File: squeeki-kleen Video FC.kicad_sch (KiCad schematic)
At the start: 11 parts, among them J1 VCC, J2 VOUT, J3 GND, J4 Conn_Coaxial, Q1 MMBT3906

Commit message: Add version number to PCB
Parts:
- J4: now left out of the parts list
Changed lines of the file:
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@@
   )
   (symbol (lib_id "Connector:Conn_Coaxial") (at 105.41 31.75 0) (unit 1)
-    (in_bom yes) (on_board yes) (dnp no) (fields_autoplaced)
+    (in_bom no) (on_board yes) (dnp no) (fields_autoplaced)
     (property "Reference" "J4" (at 107.95 30.7731 0)
       (effects (font (size 1.27 1.27)) (justify left))

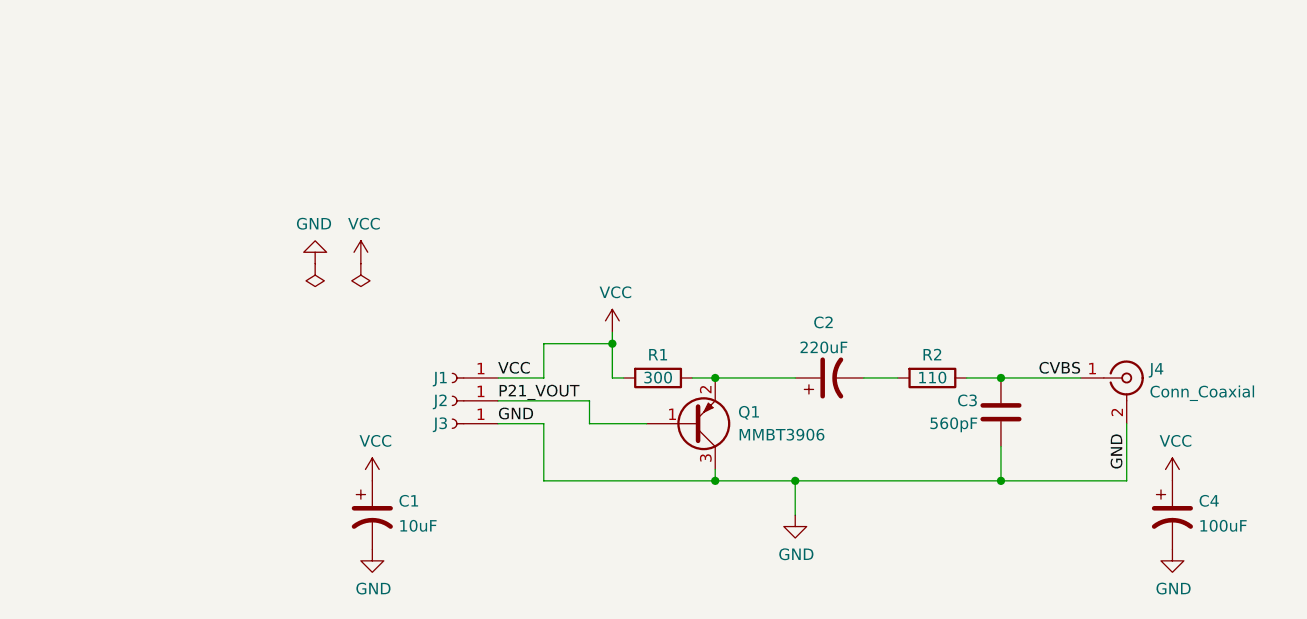
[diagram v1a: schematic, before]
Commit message: Compact component placement, add teardrops
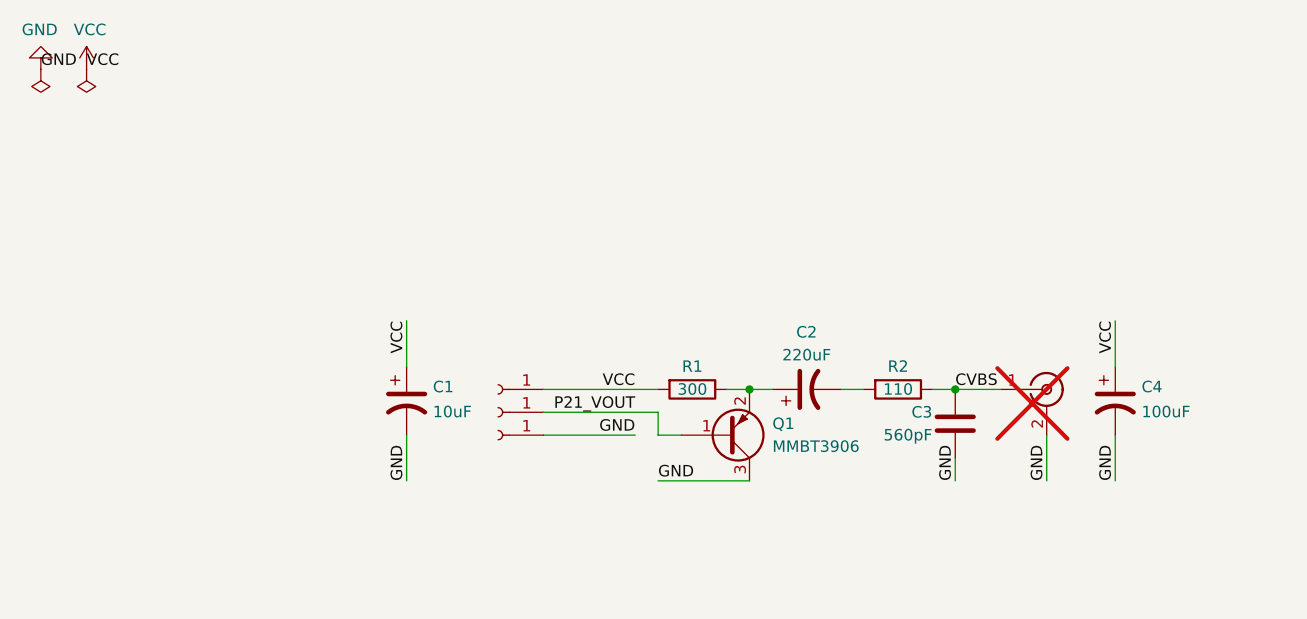
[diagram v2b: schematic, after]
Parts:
- C1: footprint Capacitor_Tantalum_SMD:CP_EIA-3216-18_Kemet-A_Pad1.58x1.35mm_HandSolder -> Capacitor_Tantalum_SMD:CP_EIA-3216-18_Kemet-A
- C3: footprint Capacitor_SMD:C_0805_2012Metric_Pad1.18x1.45mm_HandSolder -> Capacitor_SMD:C_0805_2012Metric
- C4: LCSC C1508940 -> C5374788
- J1, J2, J3: now left out of the parts list
- J4: now not fitted
- Q1: LCSC (none) -> C2891809
- R1, R2: footprint Resistor_SMD:R_0805_2012Metric_Pad1.20x1.40mm_HandSolder -> Resistor_SMD:R_0805_2012Metric
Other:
- moved on the sheet: C1, C2, C3, C4, Q1, R1, R2

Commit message: Widen holes, add extra empty capacitor footprints
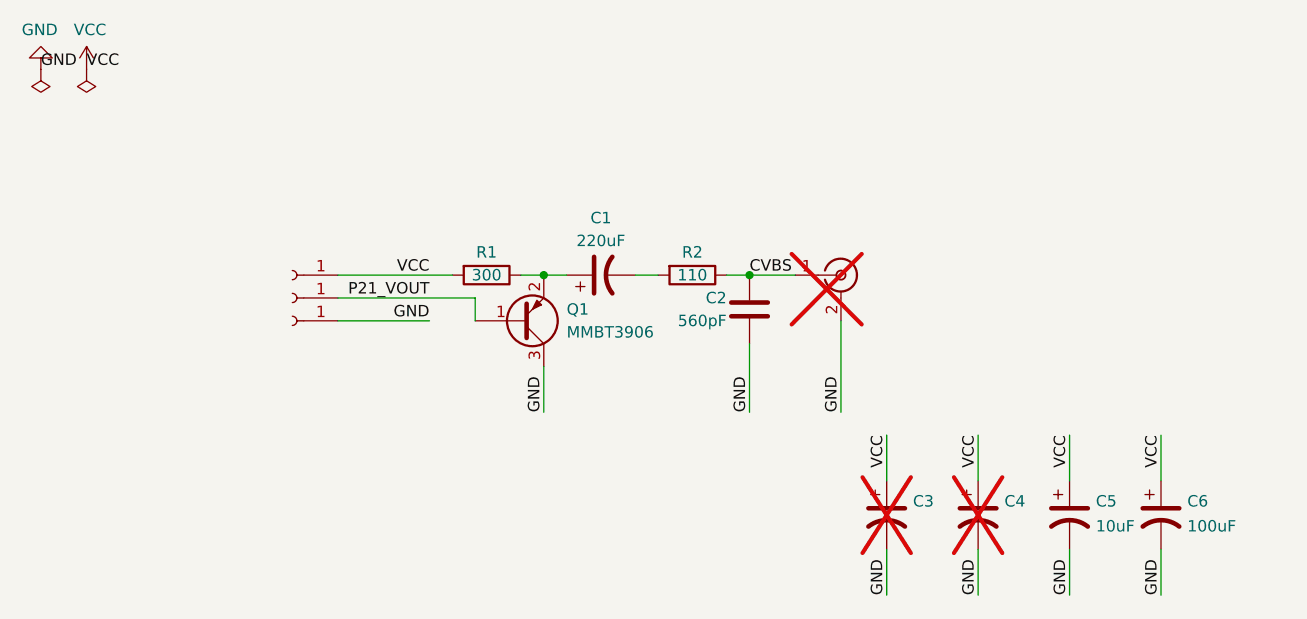
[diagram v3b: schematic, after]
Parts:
- added C3, C4: ~, Capacitor_Tantalum_SMD:CP_EIA-3216-18_Kemet-A, symbol Device:C_Polarized_US
- renumbered C2 to C1, C3 to C2, C1 to C5, C4 to C6
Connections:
- net GND: now also C3.2, C4.2
- net VCC: now also C3.1, C4.1
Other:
- moved on the sheet: C1, C2, C5, C6, Q1, R1, R2
